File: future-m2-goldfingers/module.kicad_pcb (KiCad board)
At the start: 4 copper layers, 22 x 42 mm, 44 parts, among them J1 M.2 Key M card edge (custom p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, J3 U.FL-R-SMT-1(01), U1 ESP32-C6FH8, U2 iCE40UP5K-SG48, U3 TLV75512PDBVR, Y1 40MHz / CL10pF

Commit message: Remove the 12 stray stitching vias and let lint catch future ones
Twelve free-standing GND vias (the "plane stitching" list, including
the one at 121.3, 106.8) touched no trace or pad. Lint never flagged
them because the route script labelled every unattached ground via
"stitching" (and any via within 1.6 mm of a capacitor ground pad
"return") in the lint role map. Without those labels lint reports them
as via.role_missing.

The vias are gone, and roles are now assigned only to vias that a
same-net trace touches (return / feed) or that sit in an exposed pad
(thermal). Anything else stays unroled, so lint reports it.

DRC with parity 0 and no isolated copper (every outer ground-pour
island still reaches In1 through an attached via), ERC 0, lint 24
infos with no via.role_missing, quality unchanged.

Co-Authored-By: Claude Opus 5.5 <noreply@anthropic.com>
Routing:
- net GND: vias 59 -> 47

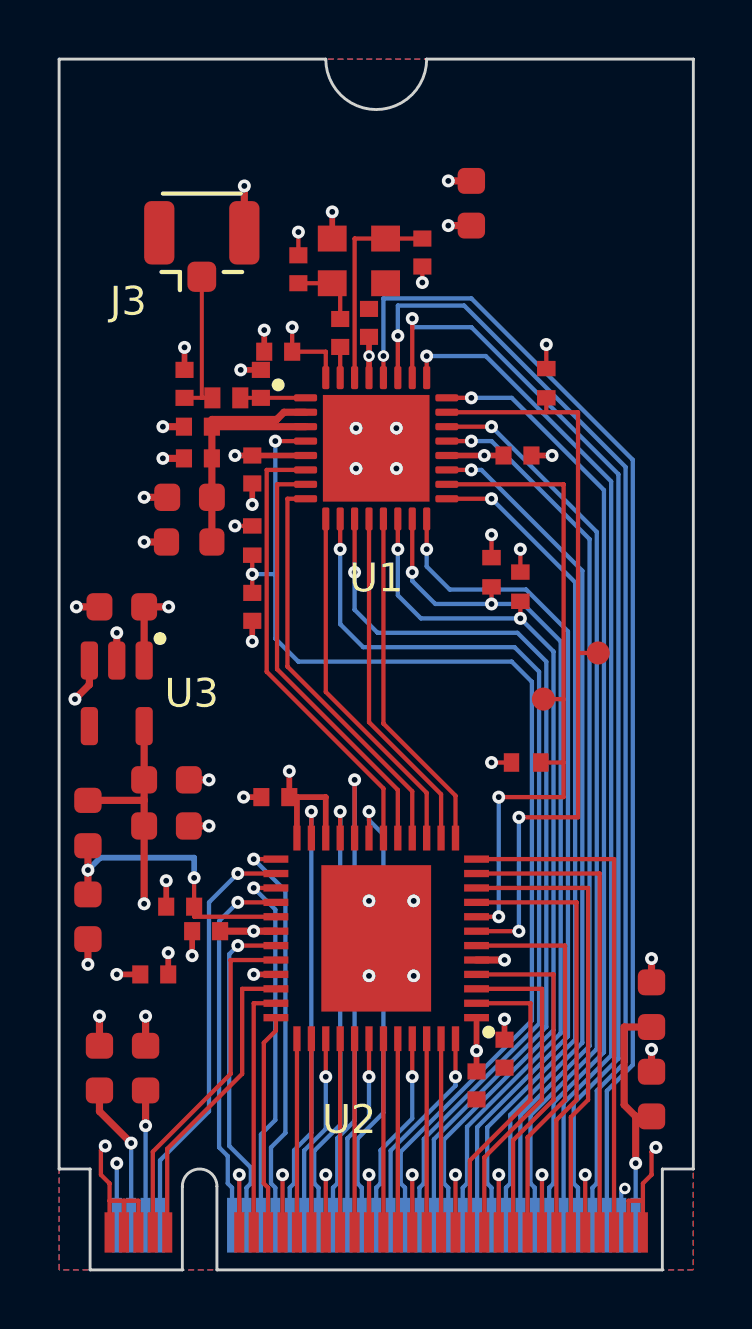
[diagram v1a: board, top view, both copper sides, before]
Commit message: Move the v2 module to the QFN40 ESP32-C6 with a 16 MB flash
U1 is now the flashless ESP32-C6 in QFN40 (LCSC C5364646, 0.4 mm pitch,
3.3 mm exposed pad; KiCad's QFN-40 land with the pad shrunk to match),
with a Winbond W25Q128JVPIQ 16 MB quad SPI flash (U4, LCSC C190862)
on SPI0/1 in QIO mode.

Pin changes: the QFN40 has GPIO10/11 but no GPIO14, so CRESET/CDONE
move to GPIO10/11 and GPIO18 is new on the connector (13 GPIOs + USB +
EN). The ESP bus grows to 16 back lanes; contact 33 (formerly ground)
carries GPIO4 through its old via, and the other ESP contacts shift one
slot east (USB is now on 26/24).

Layout: U1 moved 0.5 mm south to make room for the crystal's 0201 L5
and the 0201 VDDA1 cap. U4 sits in the north-east corner, rotated so
DI/CLK/HOLD fan straight into its south row; WP/DO/CS run up the east
side and WP/DO cross under CS on B.Cu above the chip (the flash pin
order is mirrored against the C6's). The flash runs from the 3.3 V
plane and VDD_SPI is left unconnected (it sits between the flash pins);
C68 0.1 uF decouples pin 8, C33 10 uF is 4 mm away. VDDPST2's plane and
ground vias sit on midlines between the B.Cu bus legs.

ERC 0, DRC with parity 0, lint 35 infos (no warnings), quality errors
31 (same accepted categories). New decoupling deviations recorded:
VDDPST1 2.7 mm, VDDPST2 2.4 mm, VDDA3P3 3.6 mm. L5 (24 nH 0201) still
needs an LCSC number.

Co-Authored-By: Claude Opus 5.5 <noreply@anthropic.com>
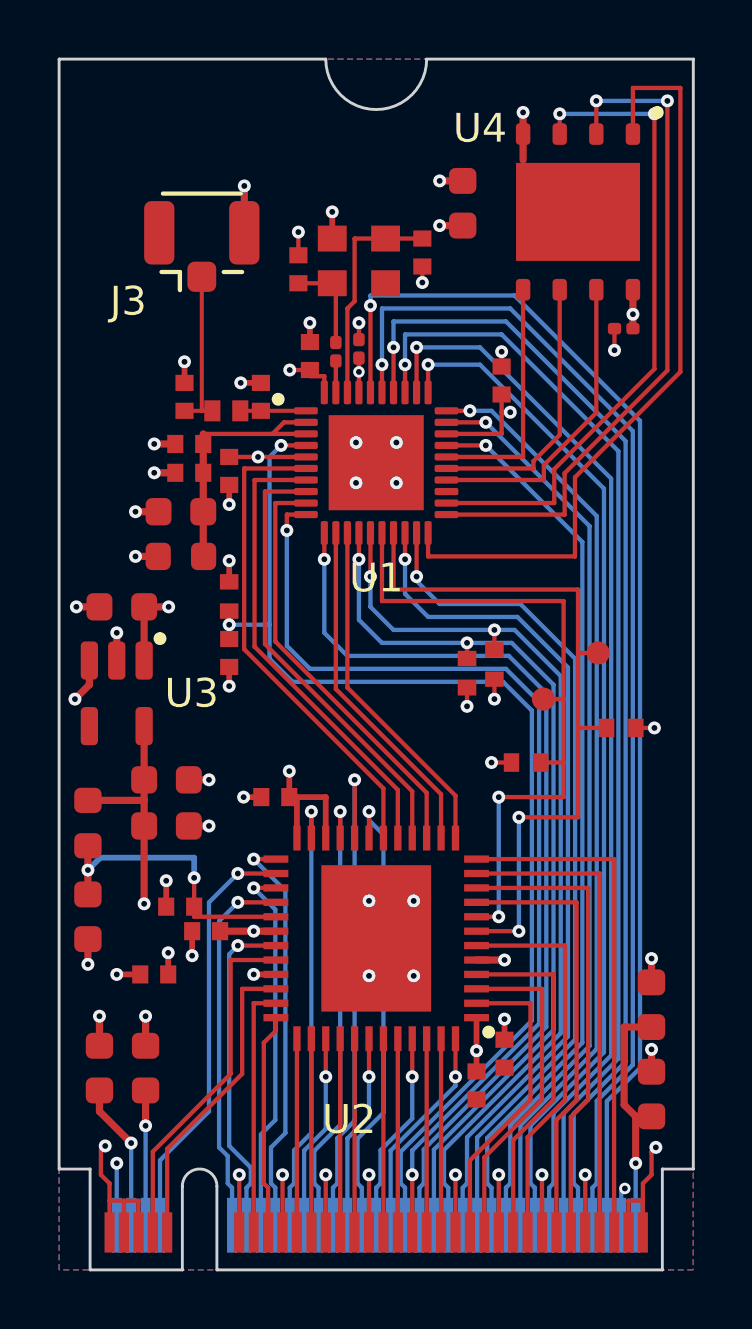
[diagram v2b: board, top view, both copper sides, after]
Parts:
- added C68: 0.1uF, Module2:C_0201, F.Cu at (119.6, 109.3)
- added U4: W25Q128JVPIQ, Module2:WSON-8-1EP_6x5mm_P1.27mm_EP3.4x4.3mm, F.Cu at (118.0, 105.3)
- C39: footprint Module2:C_0402 -> Module2:C_0201
- L5: footprint Module2:C_0402 -> Module2:L_0201
- U1: value ESP32-C6FH8 -> ESP32-C6; footprint Module2:QFN-32-1EP_5x5mm_P0.5mm_EP3.7x3.7mm -> Module2:QFN-40-1EP_5x5mm_P0.4mm_EP3.3x3.3mm
- moved R29 12.2 mm to (119.5, 123.2), turned to 0 degrees
- moved R21 3.52 mm to (114.2, 121.3), turned to -90 degrees
- moved R20 3.20 mm to (115.1, 121.0), turned to -90 degrees
- moved C38 2.66 mm to (115.3, 111.2), turned to 90 degrees
- moved R22 2.10 mm to (105.9, 118.6)
- moved C32 1.79 mm to (105.9, 120.6)
- moved C40 1.11 mm to (108.7, 110.3), turned to 90 degrees
- moved C39 0.97 mm to (110.4, 110.0)
- moved C37 0.80 mm to (105.9, 114.3)
- moved C35 0.67 mm to (104.5, 113.3)
- moved L5 0.67 mm to (109.6, 110.2)
- moved C34 0.58 mm to (104.2, 115.7)
- moved C36 0.58 mm to (104.5, 114.3)
- moved L1 0.58 mm to (104.2, 117.2)
- moved U1 0.50 mm to (111.0, 114.0)
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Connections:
- J1 pad 16: ESP_GPIO17_RXD -> ESP_GPIO18
- J1 pad 18: ESP_GPIO16_TXD -> ESP_GPIO17_RXD
- J1 pad 20: ESP_GPIO15 -> ESP_GPIO16_TXD
- J1 pad 22: USB_D+ -> ESP_GPIO15
- J1 pad 24: USB_D- -> USB_D+
- J1 pad 26: ESP_GPIO9_BOOT -> USB_D-
- J1 pad 28: ESP_GPIO8 -> ESP_GPIO9_BOOT
- J1 pad 30: ESP_GPIO5 -> ESP_GPIO8
- J1 pad 32: ESP_GPIO4 -> ESP_GPIO5
- J1 pad 33: GND -> ESP_GPIO4
- U1 pad 16: USB_D- -> FPGA_CRESET_N
- U1 pad 17: USB_D+ -> FPGA_CDONE
- U1 pad 18: FPGA_CRESET_N -> USB_D-
- U1 pad 19: ESP_GPIO15 -> USB_D+
- U1 pad 20: +3.3V -> FLASH_CS
- U1 pad 21: ESP_GPIO16_TXD -> FLASH_DO
- U1 pad 22: ESP_GPIO17_RXD -> FLASH_WP
- U1 pad 23: FPGA_CDONE -> unconnected-(U1-VDD_SPI-Pad23)
- U1 pad 24: ESP_GPIO19 -> FLASH_HD
- U1 pad 25: ESP_GPIO20 -> FLASH_CLK
- U1 pad 26: ESP_GPIO21 -> FLASH_DI
- U1 pad 27: ESP_GPIO22 -> ESP_GPIO15
- U1 pad 28: ESP_GPIO23 -> +3.3V
- U1 pad 29: +3.3V -> ESP_GPIO16_TXD
- U1 pad 30: XTAL_N -> ESP_GPIO17_RXD
- U1 pad 31: XTAL_P -> ESP_GPIO18
- U1 pad 32: +3.3V -> ESP_GPIO19
- U1 pad 33: GND -> ESP_GPIO20
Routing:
- net ESP_GPIO18: track 0.00 -> 35.5 mm, vias 0 -> 1
- net FLASH_CS: track 0.00 -> 26.9 mm
- net FLASH_DO: track 0.00 -> 23.5 mm, vias 0 -> 2
- net FLASH_WP: track 0.00 -> 22.7 mm, vias 0 -> 2
- net FLASH_HD: track 0.00 -> 10.7 mm
- net FLASH_CLK: track 0.00 -> 9.59 mm
- net FLASH_DI: track 0.00 -> 8.46 mm
- net ESP_GPIO19: track 33.1 -> 37.0 mm
- net ESP_GPIO20: track 35.4 -> 38.7 mm
- net ESP_GPIO4: track 32.2 -> 35.0 mm, vias 1 -> 2
- net FPGA_SPI_SCK: track 12.5 -> 14.9 mm
- net ESP_GPIO23: track 40.6 -> 42.9 mm
- net ESP_GPIO22: track 39.5 -> 41.5 mm
- net ESP_GPIO21: track 38.4 -> 40.2 mm
- net FPGA_CDONE: track 27.3 -> 25.4 mm
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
